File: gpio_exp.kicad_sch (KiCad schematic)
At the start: 17 parts, among them U10 PCA9534BS_QFN

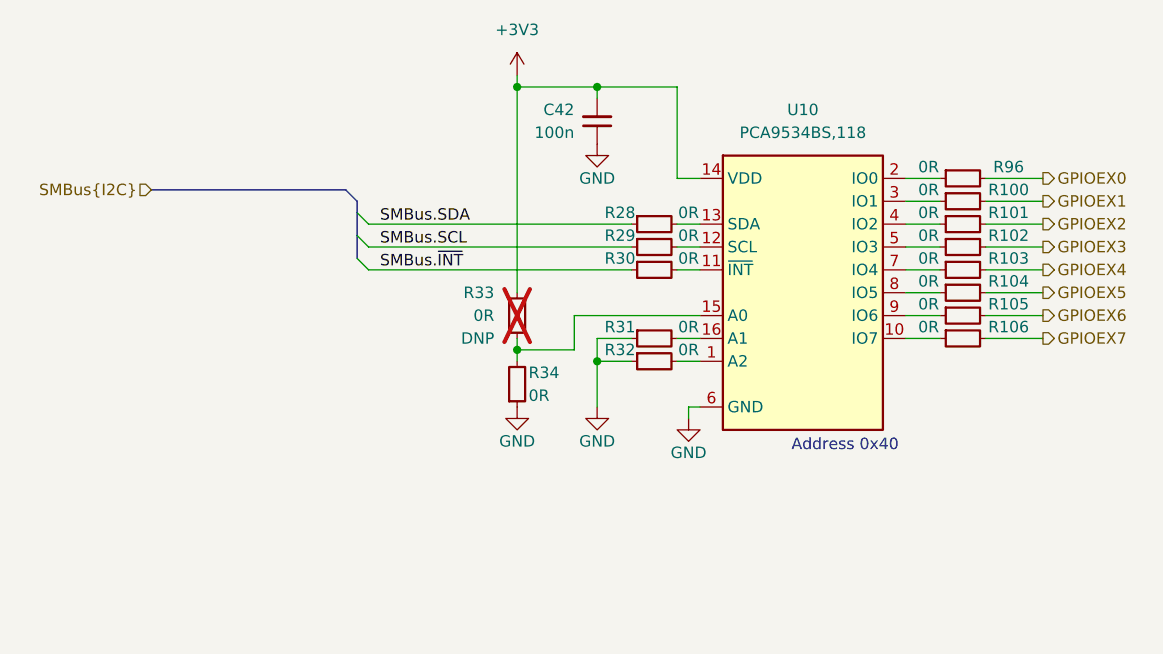
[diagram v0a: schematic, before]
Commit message: [#57498] Add SFP+ indicator LEDs
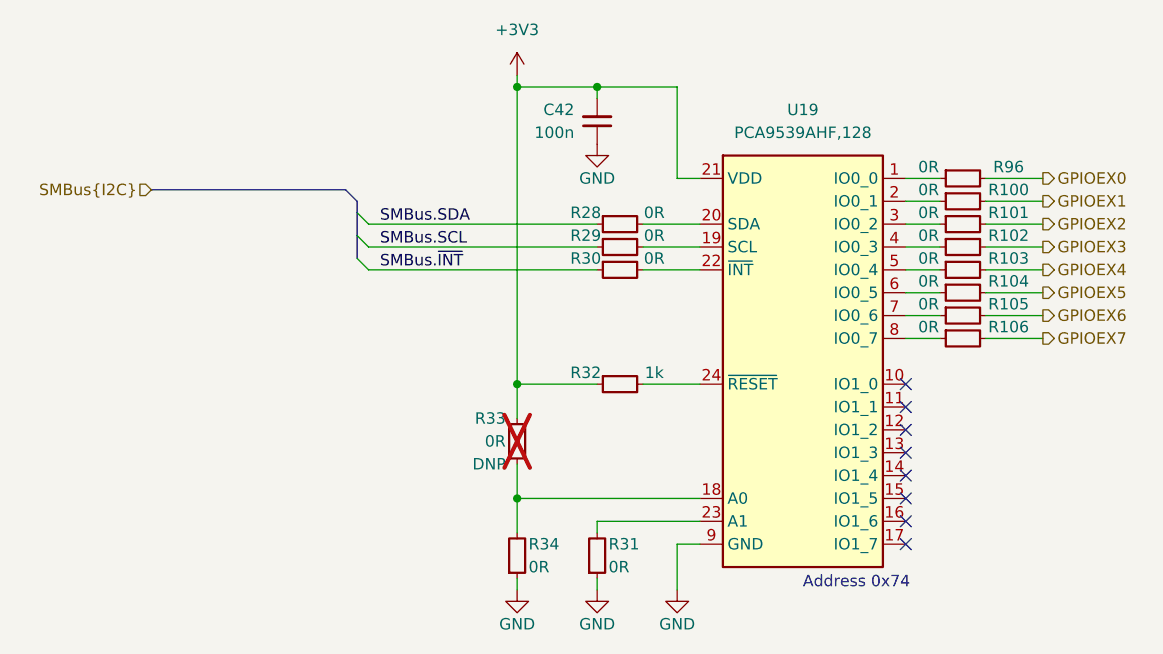
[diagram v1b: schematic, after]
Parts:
- removed R32: R_0R_0402, antmicro-footprints:R_0402_1005Metric, symbol antmicroResistors0402:R_0R_0402
- removed U10: PCA9534BS_QFN, antmicro-footprints:QFN-16-1EP_4x4mm_P0.65mm, symbol antmicroInterfaceIOExpanders:PCA9534BS_QFN
- added R32: R_1k_0402, antmicro-footprints:R_0402_1005Metric, symbol antmicroResistors0402:R_1k_0402
- added U19: PCA9539AHF, antmicro-footprints:QFN-24-1EP_4x4mm_P0.5_EP2.1x2.1mm, symbol antmicroInterfaceIOExpanders:PCA9539AHF
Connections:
- net +3V3: now also R32.1, U19.21 (VDD)
- net GND: now also U19.25 (GND), U19.9 (GND)
- net at R106.1: now also U19.8 (IO0_7)
- net at R102.1: now also U19.4 (IO0_3)
- net at R101.1: now also U19.3 (IO0_2)
- net at R30.2: now also U19.22 (~{INT})
- net at R29.2: now also U19.19 (SCL)
- net at R28.2: now also U19.20 (SDA)
- net at R33.1, R34.2: now also U19.18 (A0)
- net at R31.2: now also U19.23 (A1)
- net at R96.1: now also U19.1 (IO0_0)
- net at R100.1: now also U19.2 (IO0_1)
- net at R103.1: now also U19.5 (IO0_4)
- net at R104.1: now also U19.6 (IO0_5)
- net at R105.1: now also U19.7 (IO0_6)
- new net: R32.2, U19.24 (~{RESET})
- no-connect marks 0 -> 8
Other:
- note added: "Address 0x74"
- note removed: "Address 0x40"
- moved on the sheet: R28, R29, R30, R31, R33, R34

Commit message: [#58137] Update backplane connector pinout
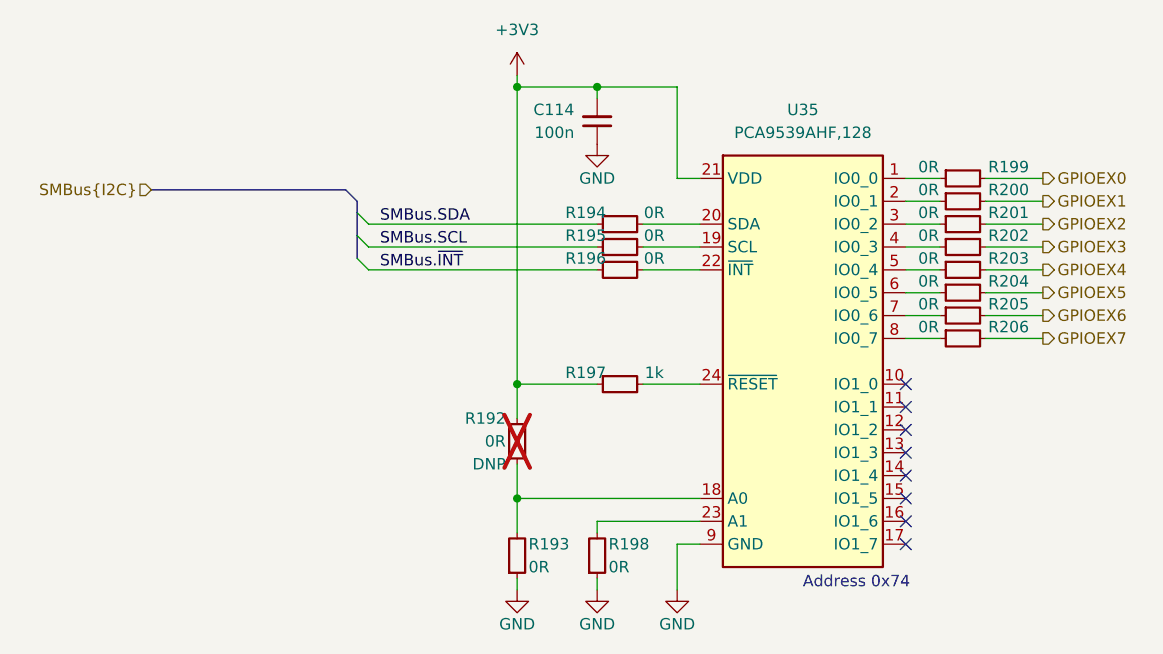
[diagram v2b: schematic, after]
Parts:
- renumbered C42 to C114, R33 to R192, R34 to R193, R28 to R194, R29 to R195, R30 to R196, R32 to R197, R31 to R198, R96 to R199, R100 to R200, R101 to R201, R102 to R202, R103 to R203, R104 to R204, R105 to R205, R106 to R206, U19 to U35

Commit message: [#58137] Add power sequencing and reset
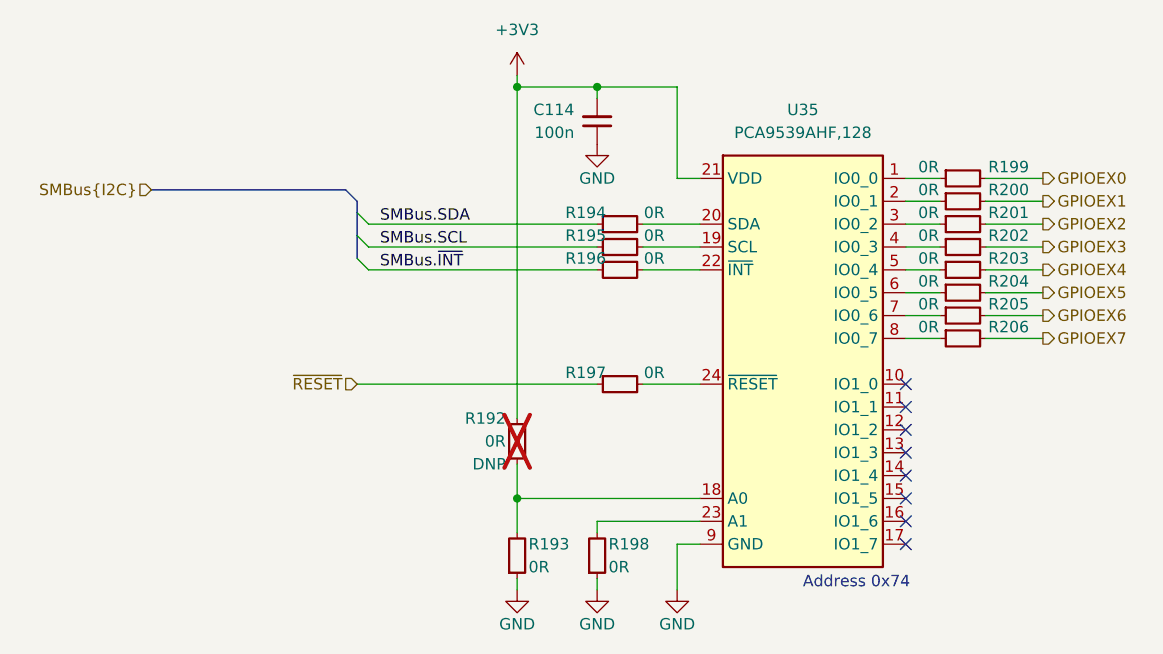
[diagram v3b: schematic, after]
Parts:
- removed R197: R_1k_0402, antmicro-footprints:R_0402_1005Metric, symbol antmicroResistors0402:R_1k_0402
- added R197: R_0R_0402, antmicro-footprints:R_0402_1005Metric, symbol antmicroResistors0402:R_0R_0402
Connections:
- net at U35.24 (~{RESET}): now also R197.2
- new net ~{RESET}: R197.1
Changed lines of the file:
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@@
   (junction (at 180.34 167.64) (diameter 0) (color 0 0 0 0)
-  )
-  (junction (at 180.34 154.94) (diameter 0) (color 0 0 0 0)
   )
   (junction (at 189.23 121.92) (diameter 0) (color 0 0 0 0)
@@
     (stroke (width 0) (type default))
   )
+  (wire (pts (xy 162.56 154.94) (xy 189.23 154.94))
+    (stroke (width 0) (type default))
+  )
   (wire (pts (xy 163.83 139.7) (xy 189.23 139.7))
     (stroke (width 0) (type default))
@@
     (stroke (width 0) (type default))
   )
-  (wire (pts (xy 180.34 158.75) (xy 180.34 154.94))
-    (stroke (width 0) (type default))
-  )
-  (wire (pts (xy 180.34 154.94) (xy 180.34 121.92))
+  (wire (pts (xy 194.31 154.94) (xy 200.66 154.94))
+    (stroke (width 0) (type default))
+  )
+  (wire (pts (xy 180.34 121.92) (xy 180.34 158.75))
     (stroke (width 0) (type default))
   )
@@
     (stroke (width 0) (type default))
   )
-  (wire (pts (xy 180.34 154.94) (xy 189.23 154.94))
-    (stroke (width 0) (type default))
-  )
   (wire (pts (xy 198.12 132.08) (xy 200.66 132.08))
     (stroke (width 0) (type default))
@@
   )
   (wire (pts (xy 227.33 144.78) (xy 223.52 144.78))
-    (stroke (width 0) (type default))
-  )
-  (wire (pts (xy 194.31 154.94) (xy 200.66 154.94))
     (stroke (width 0) (type default))
   )
@@
     (effects (font (size 1.27 1.27)) (justify left))
   )
+  (hierarchical_label "~{RESET}" (shape input) (at 162.56 154.94 180) (fields_autoplaced)
+    (effects (font (size 1.27 1.27)) (justify right))
+  )
   (symbol (lib_id "antmicroResistors0402:R_0R_0402") (at 227.33 149.86 0) (unit 1)
     (in_bom yes) (on_board yes) (dnp no)
@@
     )
   )
+  (symbol (lib_id "antmicroResistors0402:R_0R_0402") (at 189.23 154.94 0) (unit 1)
+    (in_bom yes) (on_board yes) (dnp no)
+    (property "Reference" "R197" (at 187.96 153.67 0)
+      (effects (font (size 1.27 1.27) (thickness 0.15)))
+    )
+    (property "Value" "R_0R_0402" (at 209.55 167.64 0)
+      (effects (font (size 1.27 1.27) (thickness 0.15)) (justify left bottom) hide)
+    )
+    (property "Footprint" "antmicro-footprints:R_0402_1005Metric" (at 209.55 170.18 0)
+      (effects (font (size 1.27 1.27) (thickness 0.15)) (justify left bottom) hide)
+    )
+    (property "Datasheet" "https://industrial.panasonic.com/cdbs/www-data/pdf/RDA0000/AOA0000C301.pdf" (at 209.55 172.72 0)
+      (effects (font (size 1.27 1.27) (thickness 0.15)) (justify left bottom) hide)
+    )
+    (property "MPN" "ERJ2GE0R00X" (at 209.55 175.26 0)
+      (effects (font (size 1.27 1.27) (thickness 0.15)) (justify left bottom) hide)
+    )
+    (property "Manufacturer" "Panasonic" (at 209.55 177.8 0)
+      (effects (font (size 1.27 1.27) (thickness 0.15)) (justify left bottom) hide)
+    )
+    (property "License" "Apache-2.0" (at 209.55 180.34 0)
+      (effects (font (size 1.27 1.27) (thickness 0.15)) (justify left bottom) hide)
+    )
+    (property "Author" "Antmicro" (at 209.55 182.88 0)
+      (effects (font (size 1.27 1.27) (thickness 0.15)) (justify left bottom) hide)
+    )
+    (property "Val" "0R" (at 195.58 153.67 0)
+      (effects (font (size 1.27 1.27) (thickness 0.15)))
+    )
+    (property "Tolerance" "~" (at 209.55 165.1 0)
+      (effects (font (size 1.27 1.27)) (justify left bottom) hide)
+    )
+    (property "Current" "1A" (at 209.55 185.42 0)
+      (effects (font (size 1.27 1.27) (thickness 0.15)) (justify left bottom) hide)
+    )
+    (pin "1")
+    (pin "2")
+    (instances
+      (project "com-express-7-baseboard"
+        (path "/1b8c34da-dad5-4b0b-8c4b-45db766c4dfa/50145e18-6fda-4310-8f05-c3e546b9d1d3"
+          (reference "R197") (unit 1)
+        )
+      )
+    )
+  )
   (symbol (lib_id "antmicroResistors0402:R_0R_0402") (at 189.23 139.7 0) (unit 1)
     (in_bom yes) (on_board yes) (dnp no)
@@
         )
       )
-    )
-  )
-  (symbol (lib_id "antmicroResistors0402:R_1k_0402") (at 189.23 154.94 0) (unit 1)
-    (in_bom yes) (on_board yes) (dnp no)
-    (property "Reference" "R197" (at 187.96 153.67 0)
-      (effects (font (size 1.27 1.27) (thickness 0.15)))
-    )
-    (property "Value" "R_1k_0402" (at 209.55 167.64 0)
-      (effects (font (size 1.27 1.27) (thickness 0.15)) (justify left bottom) hide)
-    )
-    (property "Footprint" "antmicro-footprints:R_0402_1005Metric" (at 209.55 170.18 0)
-      (effects (font (size 1.27 1.27) (thickness 0.15)) (justify left bottom) hide)
-    )
-    (property "Datasheet" "https://www.bourns.com/docs/product-datasheets/cr.pdf" (at 209.55 172.72 0)
-      (effects (font (size 1.27 1.27) (thickness 0.15)) (justify left bottom) hide)
-    )
-    (property "MPN" "CR0402-FX-1001GLF" (at 209.55 175.26 0)
-      (effects (font (size 1.27 1.27) (thickness 0.15)) (justify left bottom) hide)
-    )
-    (property "Manufacturer" "Bourns" (at 209.55 177.8 0)
-      (effects (font (size 1.27 1.27) (thickness 0.15)) (justify left bottom) hide)
-    )
-    (property "License" "Apache-2.0" (at 209.55 180.34 0)
-      (effects (font (size 1.27 1.27) (thickness 0.15)) (justify left bottom) hide)
-    )
-    (property "Author" "Antmicro" (at 209.55 182.88 0)
-      (effects (font (size 1.27 1.27) (thickness 0.15)) (justify left bottom) hide)
-    )
-    (property "Val" "1k" (at 195.58 153.67 0)
-      (effects (font (size 1.27 1.27) (thickness 0.15)))
-    )
-    (property "Tolerance" "1%" (at 209.55 165.1 0)
-      (effects (font (size 1.27 1.27)) (justify left bottom) hide)
-    )
-    (pin "2")
-    (pin "1")
-    (instances
-      (project "com-express-7-baseboard"
-        (path "/1b8c34da-dad5-4b0b-8c4b-45db766c4dfa/50145e18-6fda-4310-8f05-c3e546b9d1d3"
-          (reference "R197") (unit 1)
-        )
-      )

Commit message: Reannotate schematic
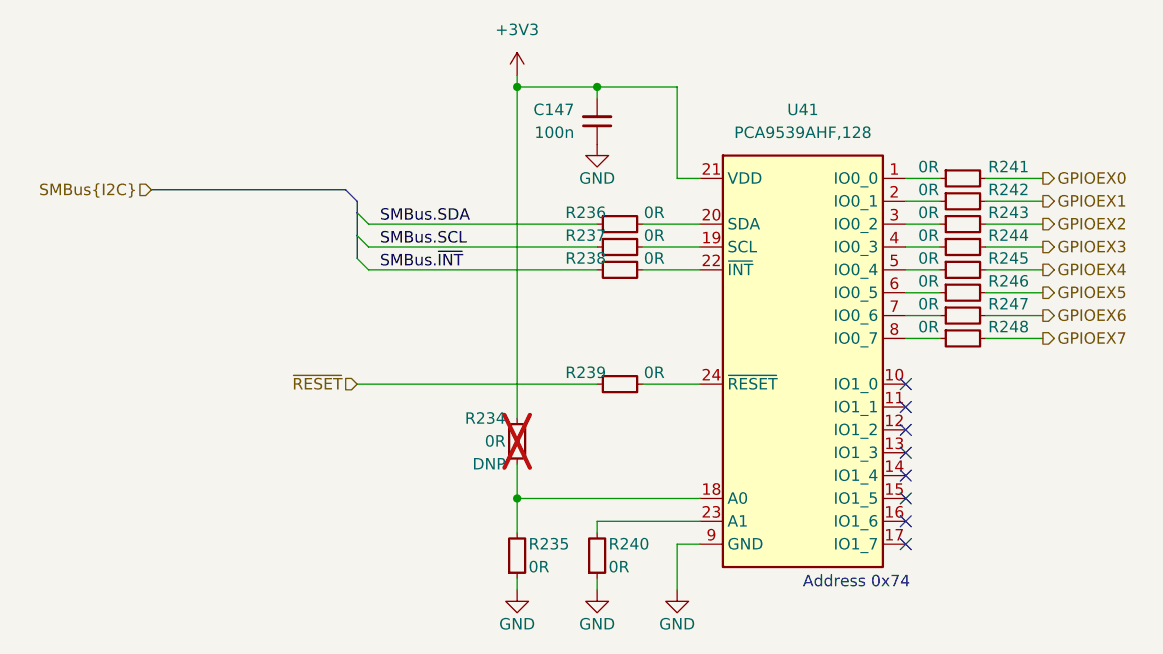
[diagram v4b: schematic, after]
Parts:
- renumbered C114 to C147, R192 to R234, R193 to R235, R194 to R236, R195 to R237, R196 to R238, R197 to R239, R198 to R240, R199 to R241, R200 to R242, R201 to R243, R202 to R244, R203 to R245, R204 to R246, R205 to R247, R206 to R248, U35 to U41

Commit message: Optimize BOM, reannotate
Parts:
- renumbered R234 to R231, R235 to R232, R236 to R233, R237 to R234, R238 to R235, R239 to R236, R240 to R237, R241 to R238, R242 to R239, R243 to R240, R244 to R241, R245 to R242, R246 to R243, R247 to R244, R248 to R245
